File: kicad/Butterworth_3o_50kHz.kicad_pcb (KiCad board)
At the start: 2 copper layers, 40.6 x 48.5 mm, 30 parts, among them J1 Conn_01x02_Pin, J2 Conn_01x02_Pin, J3 Conn_01x03_Pin, J4 Conn_01x02_Pin, J5 Conn_01x02_Pin, J6 Conn_01x02_Pin, J7 Conn_01x02_Pin, U1 TL072, U2 LM317L_TO92, U3 LMC7660

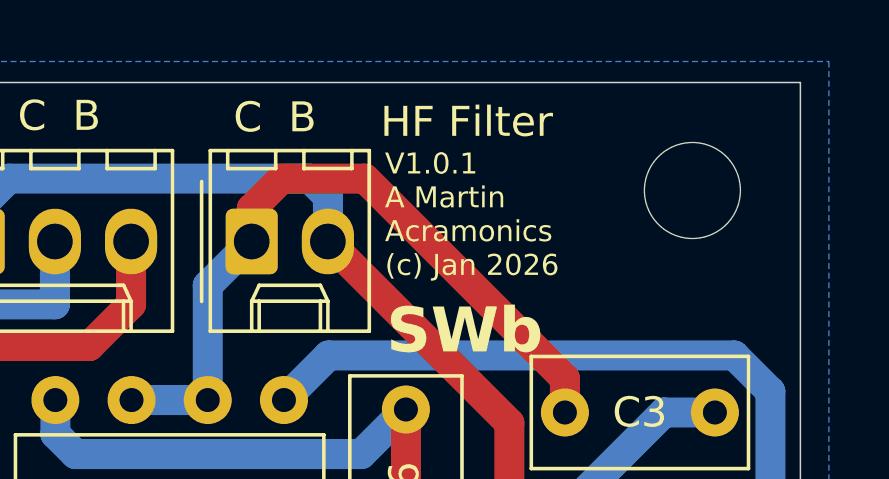
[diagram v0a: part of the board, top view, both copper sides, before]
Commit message: Corrected filenames to 50kHz instead of 40kHz
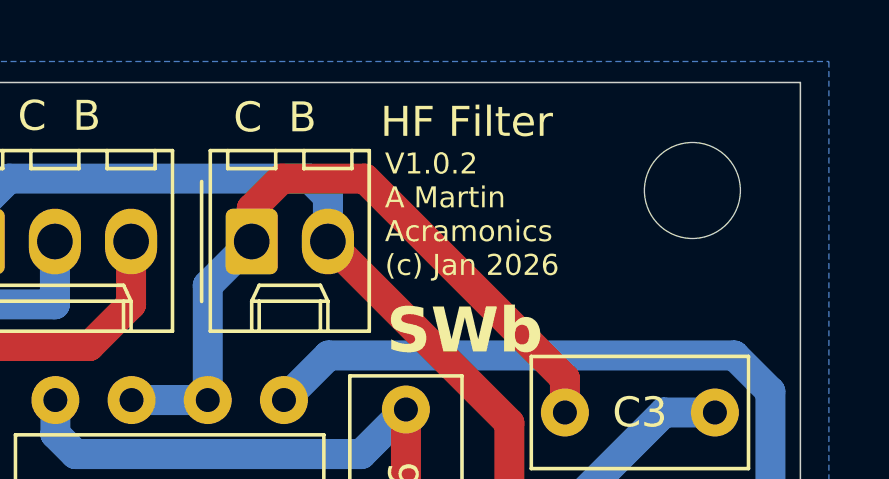
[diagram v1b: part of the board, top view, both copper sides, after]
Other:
- board text added: "V1.0.2 A Martin Acramonics (c) Jan 2026"
- board text removed: "V1.0.1 A Martin Acramonics (c) Jan 2026"
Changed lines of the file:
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@@
 		(property ki_fp_filters "SOIC*3.9x4.9mm*P1.27mm* DIP*W7.62mm* TO*99* OnSemi*Micro8* TSSOP*3x3mm*P0.65mm* TSSOP*4.4x3mm*P0.65mm* MSOP*3x3mm*P0.65mm* SSOP*3.9x4.9mm*P0.635mm* LFCSP*2x2mm*P0.5mm* *SIP* SOIC*5.3x6.2mm*P1.27mm*")
 		(sheetname "/")
-		(sheetfile "Butterworth_3o_40kHz.kicad_sch")
+		(sheetfile "Butterworth_3o_50kHz.kicad_sch")
 		(attr through_hole)
 		(fp_line
@@
 		(property ki_fp_filters "Connector*:*_1x??_*")
 		(sheetname "/")
-		(sheetfile "Butterworth_3o_40kHz.kicad_sch")
+		(sheetfile "Butterworth_3o_50kHz.kicad_sch")
 		(attr through_hole)
 		(fp_line
@@
 		(property ki_fp_filters "R_*")
 		(sheetname "/")
-		(sheetfile "Butterworth_3o_40kHz.kicad_sch")
+		(sheetfile "Butterworth_3o_50kHz.kicad_sch")
 		(attr through_hole)
 		(fp_line
@@
 		(property ki_fp_filters "R_*")
 		(sheetname "/")
-		(sheetfile "Butterworth_3o_40kHz.kicad_sch")
+		(sheetfile "Butterworth_3o_50kHz.kicad_sch")
 		(attr through_hole)
 		(fp_line
@@
 		(property ki_fp_filters "Connector*:*_1x??_*")
 		(sheetname "/")
-		(sheetfile "Butterworth_3o_40kHz.kicad_sch")
+		(sheetfile "Butterworth_3o_50kHz.kicad_sch")
 		(attr through_hole)
 		(fp_line
@@
 		(property ki_fp_filters "C_*")
 		(sheetname "/")
-		(sheetfile "Butterworth_3o_40kHz.kicad_sch")
+		(sheetfile "Butterworth_3o_50kHz.kicad_sch")
 		(attr through_hole)
 		(fp_line
@@
 		(property ki_fp_filters "C_*")
 		(sheetname "/")
-		(sheetfile "Butterworth_3o_40kHz.kicad_sch")
+		(sheetfile "Butterworth_3o_50kHz.kicad_sch")
 		(attr through_hole)
 		(fp_line
@@
 		(property ki_fp_filters "R_*")
 		(sheetname "/")
-		(sheetfile "Butterworth_3o_40kHz.kicad_sch")
+		(sheetfile "Butterworth_3o_50kHz.kicad_sch")
 		(attr through_hole)
 		(fp_line
@@
 		(property ki_fp_filters "SOIC*3.9x4.9mm*P1.27mm* DIP*W7.62mm*")
 		(sheetname "/")
-		(sheetfile "Butterworth_3o_40kHz.kicad_sch")
+		(sheetfile "Butterworth_3o_50kHz.kicad_sch")
 		(attr through_hole)
 		(fp_line
@@
 		(property ki_fp_filters "Connector*:*_1x??_*")
 		(sheetname "/")
-		(sheetfile "Butterworth_3o_40kHz.kicad_sch")
+		(sheetfile "Butterworth_3o_50kHz.kicad_sch")
 		(attr through_hole)
 		(fp_line
@@
 		(property ki_fp_filters "C_*")
 		(sheetname "/")
-		(sheetfile "Butterworth_3o_40kHz.kicad_sch")
+		(sheetfile "Butterworth_3o_50kHz.kicad_sch")
 		(attr through_hole)
 		(fp_line
@@
 		(property ki_fp_filters "Connector*:*_1x??_*")
 		(sheetname "/")
-		(sheetfile "Butterworth_3o_40kHz.kicad_sch")
+		(sheetfile "Butterworth_3o_50kHz.kicad_sch")
 		(attr through_hole)
 		(fp_line
@@
 		(property ki_fp_filters "R_*")
 		(sheetname "/")
-		(sheetfile "Butterworth_3o_40kHz.kicad_sch")
+		(sheetfile "Butterworth_3o_50kHz.kicad_sch")
 		(attr through_hole)
 		(fp_line
@@
 		(property ki_fp_filters "Connector*:*_1x??_*")
 		(sheetname "/")
-		(sheetfile "Butterworth_3o_40kHz.kicad_sch")
+		(sheetfile "Butterworth_3o_50kHz.kicad_sch")
 		(attr through_hole)
 		(fp_line
@@
 		(property ki_fp_filters "D*DO?41*")
 		(sheetname "/")
-		(sheetfile "Butterworth_3o_40kHz.kicad_sch")
+		(sheetfile "Butterworth_3o_50kHz.kicad_sch")
 		(attr through_hole)
 		(fp_line
@@
 		(property ki_fp_filters "R_*")
 		(sheetname "/")
-		(sheetfile "Butterworth_3o_40kHz.kicad_sch")
+		(sheetfile "Butterworth_3o_50kHz.kicad_sch")
 		(attr through_hole)
 		(fp_line
@@
 		(property ki_fp_filters "CP_*")
 		(sheetname "/")
-		(sheetfile "Butterworth_3o_40kHz.kicad_sch")
+		(sheetfile "Butterworth_3o_50kHz.kicad_sch")
 		(attr through_hole)
 		(fp_line
@@
 		(property ki_fp_filters "CP_*")
 		(sheetname "/")
-		(sheetfile "Butterworth_3o_40kHz.kicad_sch")
+		(sheetfile "Butterworth_3o_50kHz.kicad_sch")
 		(attr through_hole)
 		(fp_line
@@
 		(property ki_fp_filters "R_*")
 		(sheetname "/")
-		(sheetfile "Butterworth_3o_40kHz.kicad_sch")
+		(sheetfile "Butterworth_3o_50kHz.kicad_sch")
 		(attr through_hole)
 		(fp_line
@@
 		(property ki_fp_filters "TO?92*")
 		(sheetname "/")
-		(sheetfile "Butterworth_3o_40kHz.kicad_sch")
+		(sheetfile "Butterworth_3o_50kHz.kicad_sch")
 		(attr through_hole)
 		(fp_line
@@
 		(property ki_fp_filters "C_*")
 		(sheetname "/")
-		(sheetfile "Butterworth_3o_40kHz.kicad_sch")
+		(sheetfile "Butterworth_3o_50kHz.kicad_sch")
 		(attr through_hole)
 		(fp_line
@@
 		(property ki_fp_filters "Connector*:*_1x??_*")
 		(sheetname "/")
-		(sheetfile "Butterworth_3o_40kHz.kicad_sch")
+		(sheetfile "Butterworth_3o_50kHz.kicad_sch")
 		(attr through_hole)
 		(fp_line
@@
 		(property ki_fp_filters "C_*")
 		(sheetname "/")
-		(sheetfile "Butterworth_3o_40kHz.kicad_sch")
+		(sheetfile "Butterworth_3o_50kHz.kicad_sch")
 		(attr through_hole)
 		(fp_line
@@
 		(property ki_fp_filters "C_*")
 		(sheetname "/")
-		(sheetfile "Butterworth_3o_40kHz.kicad_sch")
+		(sheetfile "Butterworth_3o_50kHz.kicad_sch")
 		(attr through_hole)
 		(fp_line
@@
 		(property ki_fp_filters "R_*")
 		(sheetname "/")
-		(sheetfile "Butterworth_3o_40kHz.kicad_sch")
+		(sheetfile "Butterworth_3o_50kHz.kicad_sch")
 		(attr through_hole)
 		(fp_line
@@
 		(property ki_fp_filters "Connector*:*_1x??_*")
 		(sheetname "/")
-		(sheetfile "Butterworth_3o_40kHz.kicad_sch")
+		(sheetfile "Butterworth_3o_50kHz.kicad_sch")
 		(attr through_hole)
 		(fp_line
@@
 		)
 	)
-	(gr_text "V1.0.1\nA Martin\nAcramonics\n(c) Jan 2026"
+	(gr_text "V1.0.2\nA Martin\nAcramonics\n(c) Jan 2026"
 		(at 70.05 101.2 0)
 		(layer "F.SilkS")
